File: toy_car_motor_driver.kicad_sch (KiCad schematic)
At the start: 10 parts, among them J1 Conn_01x06_Pin, J3 Conn_01x02_Pin, J4 Screw_Terminal_01x02, J5 Screw_Terminal_01x02, J6 Screw_Terminal_01x02, U1 L293D

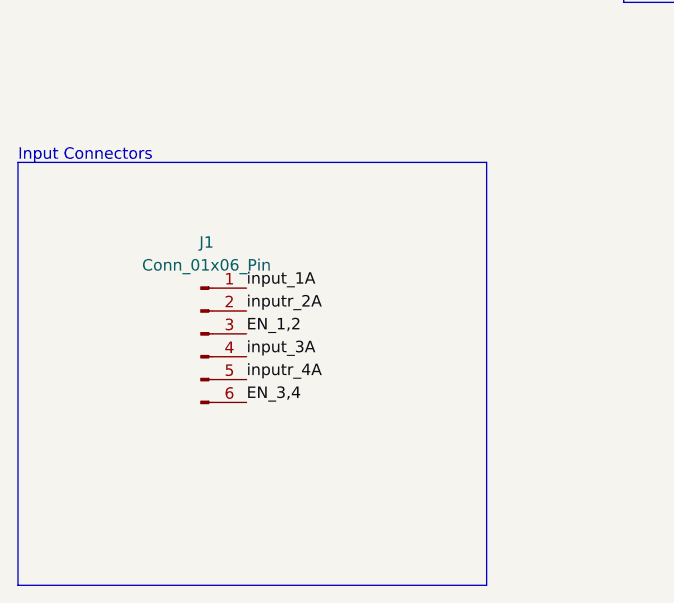
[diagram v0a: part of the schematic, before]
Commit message: added switches
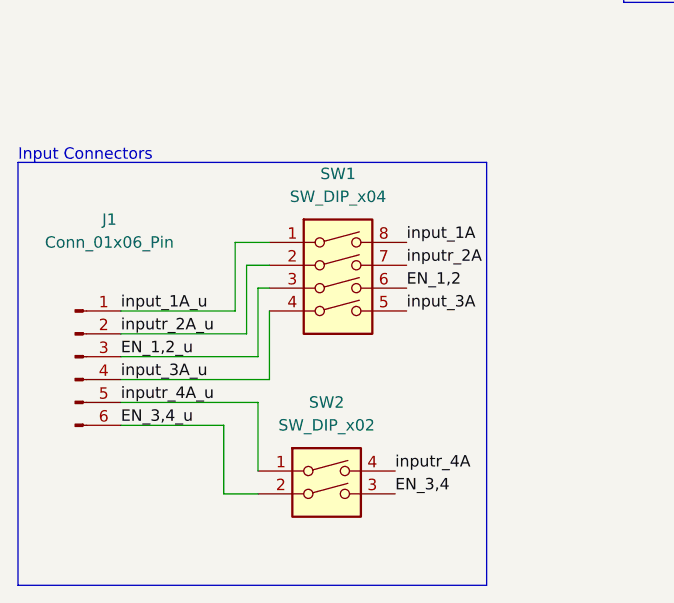
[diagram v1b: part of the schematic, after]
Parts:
- added SW1: SW_DIP_x04, symbol Switch:SW_DIP_x04
- added SW2: SW_DIP_x02, symbol Switch:SW_DIP_x02
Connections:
- net EN_1,2: now also SW1.6; no longer J1.3 (Pin_3)
- net EN_3,4: now also SW2.3; no longer J1.6 (Pin_6)
- net input_1A: now also SW1.8; no longer J1.1 (Pin_1)
- net input_3A: now also SW1.5; no longer J1.4 (Pin_4)
- net inputr_2A: now also SW1.7; no longer J1.2 (Pin_2)
- net inputr_4A: now also SW2.4; no longer J1.5 (Pin_5)
- new net EN_1,2_u: J1.3 (Pin_3), SW1.3
- new net EN_3,4_u: J1.6 (Pin_6), SW2.2
- new net input_1A_u: J1.1 (Pin_1), SW1.1
- new net input_3A_u: J1.4 (Pin_4), SW1.4
- new net inputr_2A_u: J1.2 (Pin_2), SW1.2
- new net inputr_4A_u: J1.5 (Pin_5), SW2.1
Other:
- moved on the sheet: J1
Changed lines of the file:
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@@
+    (stroke (width 0) (type default))
+  )
+  (wire (pts (xy 67.31 148.59) (xy 67.31 156.21))
     (stroke (width 0) (type default))
   )
@@
     (stroke (width 0) (type default))
   )
+  (wire (pts (xy 67.31 161.29) (xy 52.07 161.29))
+    (stroke (width 0) (type default))
+  )
   (wire (pts (xy 142.24 92.71) (xy 142.24 97.79))
     (stroke (width 0) (type default))
   )
+  (wire (pts (xy 63.5 163.83) (xy 52.07 163.83))
+    (stroke (width 0) (type default))
+  )
   (wire (pts (xy 224.79 78.74) (xy 224.79 80.01))
     (stroke (width 0) (type default))
@@
     (stroke (width 0) (type default))
   )
+  (wire (pts (xy 67.31 156.21) (xy 52.07 156.21))
+    (stroke (width 0) (type default))
+  )
   (wire (pts (xy 144.78 92.71) (xy 144.78 99.06))
     (stroke (width 0) (type default))
@@
     (stroke (width 0) (type default))
   )
+  (wire (pts (xy 67.31 168.91) (xy 67.31 161.29))
+    (stroke (width 0) (type default))
+  )
+  (wire (pts (xy 66.04 153.67) (xy 52.07 153.67))
+    (stroke (width 0) (type default))
+  )
   (wire (pts (xy 224.79 66.04) (xy 233.68 66.04))
     (stroke (width 0) (type default))
   )
+  (wire (pts (xy 67.31 171.45) (xy 63.5 171.45))
+    (stroke (width 0) (type default))
+  )
   (wire (pts (xy 139.7 104.14) (xy 139.7 101.6))
     (stroke (width 0) (type default))
   )
+  (wire (pts (xy 68.58 146.05) (xy 66.04 146.05))
+    (stroke (width 0) (type default))
+  )
   (wire (pts (xy 224.79 50.8) (xy 227.33 50.8))
     (stroke (width 0) (type default))
@@
     (stroke (width 0) (type default))
   )
+  (wire (pts (xy 68.58 148.59) (xy 67.31 148.59))
+    (stroke (width 0) (type default))
+  )
   (wire (pts (xy 142.24 39.37) (xy 142.24 41.91))
     (stroke (width 0) (type default))
@@
     (stroke (width 0) (type default))
   )
+  (wire (pts (xy 68.58 143.51) (xy 64.77 143.51))
+    (stroke (width 0) (type default))
+  )
   (wire (pts (xy 217.17 39.37) (xy 224.79 39.37))
     (stroke (width 0) (type default))
@@
     (stroke (width 0) (type default))
   )
+  (wire (pts (xy 68.58 151.13) (xy 68.58 158.75))
+    (stroke (width 0) (type default))
+  )
+  (wire (pts (xy 63.5 171.45) (xy 63.5 163.83))
+    (stroke (width 0) (type default))
+  )
+  (wire (pts (xy 68.58 158.75) (xy 52.07 158.75))
+    (stroke (width 0) (type default))
+  )
+  (wire (pts (xy 66.04 146.05) (xy 66.04 153.67))
+    (stroke (width 0) (type default))
+  )
+  (wire (pts (xy 64.77 143.51) (xy 64.77 151.13))
+    (stroke (width 0) (type default))
+  )
   (wire (pts (xy 139.7 92.71) (xy 139.7 97.79))
     (stroke (width 0) (type default))
@@
     (stroke (width 0) (type default))
   )
+  (wire (pts (xy 64.77 151.13) (xy 52.07 151.13))
+    (stroke (width 0) (type default))
+  )
   (wire (pts (xy 144.78 99.06) (xy 139.7 99.06))
     (stroke (width 0) (type default))
@@
     (effects (font (size 1.27 1.27)) (justify right bottom))
   )
-  (label "input_3A" (at 66.04 156.21 0) (fields_autoplaced)
+  (label "input_3A" (at 83.82 151.13 0) (fields_autoplaced)
+    (effects (font (size 1.27 1.27)) (justify left bottom))
+  )
+  (label "input_1A_u" (at 52.07 151.13 0) (fields_autoplaced)
     (effects (font (size 1.27 1.27)) (justify left bottom))
   )
@@
     (effects (font (size 1.27 1.27)) (justify right bottom))
   )
+  (label "EN_3,4_u" (at 52.07 163.83 0) (fields_autoplaced)
+    (effects (font (size 1.27 1.27)) (justify left bottom))
+  )
   (label "output_1" (at 152.4 57.15 0) (fields_autoplaced)
     (effects (font (size 1.27 1.27)) (justify left bottom))
   )
+  (label "inputr_4A_u" (at 52.07 161.29 0) (fields_autoplaced)
+    (effects (font (size 1.27 1.27)) (justify left bottom))
+  )
   (label "5V" (at 60.96 59.69 0) (fields_autoplaced)
     (effects (font (size 1.27 1.27)) (justify left bottom))
@@
     (effects (font (size 1.27 1.27)) (justify left bottom))
   )
-  (label "inputr_2A" (at 66.04 151.13 0) (fields_autoplaced)
+  (label "input_3A_u" (at 52.07 158.75 0) (fields_autoplaced)
+    (effects (font (size 1.27 1.27)) (justify left bottom))
+  )
+  (label "inputr_2A" (at 83.82 146.05 0) (fields_autoplaced)
     (effects (font (size 1.27 1.27)) (justify left bottom))
   )
@@
     (effects (font (size 1.27 1.27)) (justify right bottom))
   )
-  (label "EN_3,4" (at 66.04 161.29 0) (fields_autoplaced)
-    (effects (font (size 1.27 1.27)) (justify left bottom))
-  )
-  (label "input_1A" (at 66.04 148.59 0) (fields_autoplaced)
-    (effects (font (size 1.27 1.27)) (justify left bottom))
-  )
-  (label "inputr_4A" (at 66.04 158.75 0) (fields_autoplaced)
+  (label "EN_3,4" (at 82.55 171.45 0) (fields_autoplaced)
+    (effects (font (size 1.27 1.27)) (justify left bottom))
+  )
+  (label "input_1A" (at 83.82 143.51 0) (fields_autoplaced)
+    (effects (font (size 1.27 1.27)) (justify left bottom))
+  )
+  (label "inputr_4A" (at 82.55 168.91 0) (fields_autoplaced)
     (effects (font (size 1.27 1.27)) (justify left bottom))
   )
@@
     (effects (font (size 1.27 1.27)) (justify left bottom))
   )
+  (label "inputr_2A_u" (at 52.07 153.67 0) (fields_autoplaced)
+    (effects (font (size 1.27 1.27)) (justify left bottom))
+  )
   (label "outputr_1" (at 224.79 53.34 180) (fields_autoplaced)
     (effects (font (size 1.27 1.27)) (justify right bottom))
@@
     (effects (font (size 1.27 1.27)) (justify left bottom))
   )
-  (label "EN_1,2" (at 66.04 153.67 0) (fields_autoplaced)
+  (label "EN_1,2_u" (at 52.07 156.21 0) (fields_autoplaced)
+    (effects (font (size 1.27 1.27)) (justify left bottom))
+  )
+  (label "EN_1,2" (at 83.82 148.59 0) (fields_autoplaced)
     (effects (font (size 1.27 1.27)) (justify left bottom))
   )
@@
     )
   )
-  (symbol (lib_id "Connector:Conn_01x06_Pin") (at 60.96 153.67 0) (unit 1)
-    (in_bom yes) (on_board yes) (dnp no) (fields_autoplaced)
-    (property "Reference" "J1" (at 61.595 143.51 0)
-      (effects (font (size 1.27 1.27)))
-    )
-    (property "Value" "Conn_01x06_Pin" (at 61.595 146.05 0)
-      (effects (font (size 1.27 1.27)))
-    )
-    (property "Footprint" "" (at 60.96 153.67 0)
-      (effects (font (size 1.27 1.27)) hide)
-    )
-    (property "Datasheet" "~" (at 60.96 153.67 0)
+  (symbol (lib_id "Connector:Conn_01x06_Pin") (at 46.99 156.21 0) (unit 1)
+    (in_bom yes) (on_board yes) (dnp no)
+    (property "Reference" "J1" (at 50.8 140.97 0)
+      (effects (font (size 1.27 1.27)))
+    )
+    (property "Value" "Conn_01x06_Pin" (at 50.8 143.51 0)
+      (effects (font (size 1.27 1.27)))
+    )
+    (property "Footprint" "" (at 46.99 156.21 0)
+      (effects (font (size 1.27 1.27)) hide)
+    )
+    (property "Datasheet" "~" (at 46.99 156.21 0)
       (effects (font (size 1.27 1.27)) hide)
     )
@@
         (path "/bc5f8e62-44a0-4042-9de8-d5bf7b9ab401"
           (reference "#PWR05") (unit 1)
+        )
+      )
+    )
+  )
+  (symbol (lib_id "Switch:SW_DIP_x04") (at 76.2 148.59 0) (unit 1)
+    (in_bom yes) (on_board yes) (dnp no) (fields_autoplaced)
+    (property "Reference" "SW1" (at 76.2 135.89 0)
+      (effects (font (size 1.27 1.27)))
+    )
+    (property "Value" "SW_DIP_x04" (at 76.2 138.43 0)
+      (effects (font (size 1.27 1.27)))
+    )
+    (property "Footprint" "" (at 76.2 148.59 0)
+      (effects (font (size 1.27 1.27)) hide)
+    )
+    (property "Datasheet" "~" (at 76.2 148.59 0)
+      (effects (font (size 1.27 1.27)) hide)
+    )
+    (pin "3")
+    (pin "1")
+    (pin "5")
+    (pin "6")
+    (pin "4")
+    (pin "7")
+    (pin "8")
+    (pin "2")
+    (instances
+      (project "toy_car_motor_driver"
+        (path "/bc5f8e62-44a0-4042-9de8-d5bf7b9ab401"
+          (reference "SW1") (unit 1)
         )
       )
@@
         )
       )
+    )
+  )
+  (symbol (lib_id "Switch:SW_DIP_x02") (at 74.93 171.45 0) (unit 1)
+    (in_bom yes) (on_board yes) (dnp no) (fields_autoplaced)
+    (property "Reference" "SW2" (at 74.93 161.29 0)
+      (effects (font (size 1.27 1.27)))
+    )
+    (property "Value" "SW_DIP_x02" (at 74.93 163.83 0)
+      (effects (font (size 1.27 1.27)))
+    )
+    (property "Footprint" "" (at 74.93 171.45 0)
+      (effects (font (size 1.27 1.27)) hide)
+    )
+    (property "Datasheet" "~" (at 74.93 171.45 0)
+      (effects (font (size 1.27 1.27)) hide)
+    )
+    (pin "3")
+    (pin "4")
+    (pin "2")
+    (pin "1")
+    (instances
+      (project "toy_car_motor_driver"
+        (path "/bc5f8e62-44a0-4042-9de8-d5bf7b9ab401"
+          (reference "SW2") (unit 1)
+        )
+      )

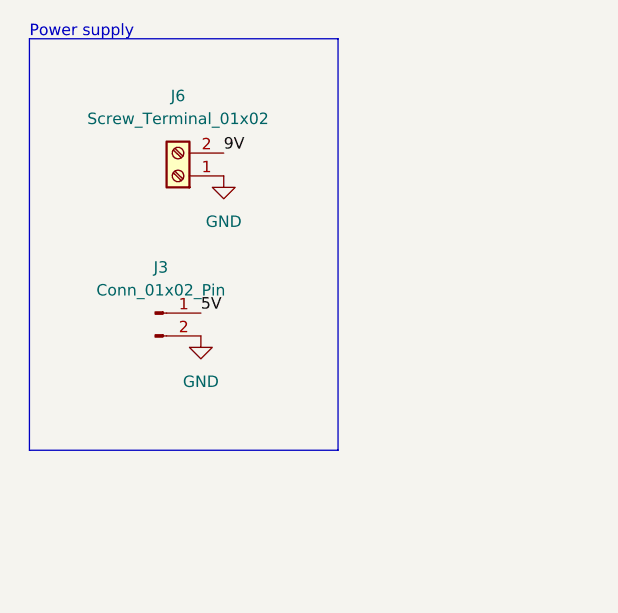
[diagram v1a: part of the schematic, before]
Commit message: Added switches for input power
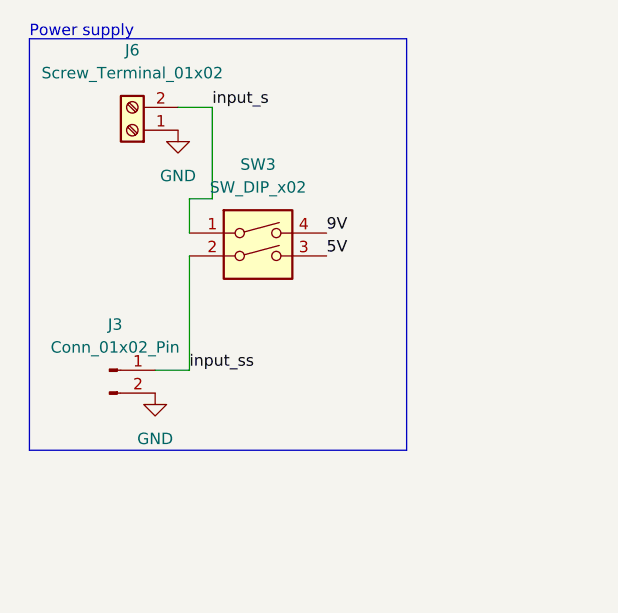
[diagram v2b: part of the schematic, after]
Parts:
- added SW3: SW_DIP_x02, symbol Switch:SW_DIP_x02
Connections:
- net 5V: now also SW3.3; no longer J3.1 (Pin_1)
- net 9V: now also SW3.4; no longer J6.2 (Pin_2)
- new net input_s: J6.2 (Pin_2), SW3.1
- new net input_ss: J3.1 (Pin_1), SW3.2
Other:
- moved on the sheet: J3, J6
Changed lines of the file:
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@@
+    (stroke (width 0) (type default))
+  )
+  (wire (pts (xy 59.69 50.8) (xy 59.69 46.99))
+    (stroke (width 0) (type default))
+  )
+  (wire (pts (xy 62.23 46.99) (xy 62.23 36.83))
+    (stroke (width 0) (type default))
+  )
+  (wire (pts (xy 58.42 36.83) (xy 62.23 36.83))
     (stroke (width 0) (type default))
   )
@@
     (stroke (width 0) (type default))
   )
+  (wire (pts (xy 59.69 46.99) (xy 62.23 46.99))
+    (stroke (width 0) (type default))
+  )
   (wire (pts (xy 68.58 146.05) (xy 66.04 146.05))
     (stroke (width 0) (type default))
@@
     (stroke (width 0) (type default))
   )
+  (wire (pts (xy 59.69 53.34) (xy 59.69 66.04))
+    (stroke (width 0) (type default))
+  )
   (wire (pts (xy 137.16 41.91) (xy 137.16 46.99))
     (stroke (width 0) (type default))
@@
     (stroke (width 0) (type default))
   )
+  (wire (pts (xy 59.69 66.04) (xy 55.88 66.04))
+    (stroke (width 0) (type default))
+  )
   (wire (pts (xy 139.7 92.71) (xy 139.7 97.79))
     (stroke (width 0) (type default))
@@
     (fill (type none))
   )
-  (rectangle (start 41.91 29.21) (end 76.2 74.93)
+  (rectangle (start 41.91 29.21) (end 83.82 74.93)
     (stroke (width 0) (type default))
     (fill (type none))
@@
     (effects (font (size 1.27 1.27)) (justify left bottom))
   )
-  (label "5V" (at 60.96 59.69 0) (fields_autoplaced)
+  (label "5V" (at 74.93 53.34 0) (fields_autoplaced)
     (effects (font (size 1.27 1.27)) (justify left bottom))
   )
@@
     (effects (font (size 1.27 1.27)) (justify left bottom))
   )
-  (label "9V" (at 63.5 41.91 0) (fields_autoplaced)
+  (label "9V" (at 74.93 50.8 0) (fields_autoplaced)
     (effects (font (size 1.27 1.27)) (justify left bottom))
   )
@@
     (effects (font (size 1.27 1.27)) (justify right bottom))
   )
+  (label "input_ss" (at 59.69 66.04 0) (fields_autoplaced)
+    (effects (font (size 1.27 1.27)) (justify left bottom))
+  )
   (label "outputr_1" (at 152.4 62.23 0) (fields_autoplaced)
     (effects (font (size 1.27 1.27)) (justify left bottom))
@@
   (label "EN_1,2" (at 127 67.31 180) (fields_autoplaced)
     (effects (font (size 1.27 1.27)) (justify right bottom))
+  )
+  (label "input_s" (at 62.23 36.83 0) (fields_autoplaced)
+    (effects (font (size 1.27 1.27)) (justify left bottom))
   )
   (label "output_2" (at 152.4 72.39 0) (fields_autoplaced)
@@
     )
   )
+  (symbol (lib_id "Switch:SW_DIP_x02") (at 67.31 53.34 0) (unit 1)
+    (in_bom yes) (on_board yes) (dnp no) (fields_autoplaced)
+    (property "Reference" "SW3" (at 67.31 43.18 0)
+      (effects (font (size 1.27 1.27)))
+    )
+    (property "Value" "SW_DIP_x02" (at 67.31 45.72 0)
+      (effects (font (size 1.27 1.27)))
+    )
+    (property "Footprint" "" (at 67.31 53.34 0)
+      (effects (font (size 1.27 1.27)) hide)
+    )
+    (property "Datasheet" "~" (at 67.31 53.34 0)
+      (effects (font (size 1.27 1.27)) hide)
+    )
+    (pin "3")
+    (pin "4")
+    (pin "2")
+    (pin "1")
+    (instances
+      (project "toy_car_motor_driver"
+        (path "/bc5f8e62-44a0-4042-9de8-d5bf7b9ab401"
+          (reference "SW3") (unit 1)
+        )
+      )
+    )
+  )
   (symbol (lib_id "Connector:Screw_Terminal_01x02") (at 232.41 50.8 0) (unit 1)
     (in_bom yes) (on_board yes) (dnp no) (fields_autoplaced)
@@
     )
   )
-  (symbol (lib_id "power:GND") (at 63.5 44.45 0) (unit 1)
-    (in_bom yes) (on_board yes) (dnp no) (fields_autoplaced)
-    (property "Reference" "#PWR03" (at 63.5 50.8 0)
-      (effects (font (size 1.27 1.27)) hide)
-    )
-    (property "Value" "GND" (at 63.5 49.53 0)
-      (effects (font (size 1.27 1.27)))
-    )
-    (property "Footprint" "" (at 63.5 44.45 0)
-      (effects (font (size 1.27 1.27)) hide)
-    )
-    (property "Datasheet" "" (at 63.5 44.45 0)
+  (symbol (lib_id "power:GND") (at 58.42 39.37 0) (unit 1)
+    (in_bom yes) (on_board yes) (dnp no) (fields_autoplaced)
+    (property "Reference" "#PWR03" (at 58.42 45.72 0)
+      (effects (font (size 1.27 1.27)) hide)
+    )
+    (property "Value" "GND" (at 58.42 44.45 0)
+      (effects (font (size 1.27 1.27)))
+    )
+    (property "Footprint" "" (at 58.42 39.37 0)
+      (effects (font (size 1.27 1.27)) hide)
+    )
+    (property "Datasheet" "" (at 58.42 39.37 0)
       (effects (font (size 1.27 1.27)) hide)
     )
@@
     )
   )
-  (symbol (lib_id "Connector:Conn_01x02_Pin") (at 55.88 59.69 0) (unit 1)
-    (in_bom yes) (on_board yes) (dnp no) (fields_autoplaced)
-    (property "Reference" "J3" (at 56.515 54.61 0)
-      (effects (font (size 1.27 1.27)))
-    )
-    (property "Value" "Conn_01x02_Pin" (at 56.515 57.15 0)
-      (effects (font (size 1.27 1.27)))
-    )
-    (property "Footprint" "" (at 55.88 59.69 0)
-      (effects (font (size 1.27 1.27)) hide)
-    )
-    (property "Datasheet" "~" (at 55.88 59.69 0)
+  (symbol (lib_id "Connector:Conn_01x02_Pin") (at 50.8 66.04 0) (unit 1)
+    (in_bom yes) (on_board yes) (dnp no) (fields_autoplaced)
+    (property "Reference" "J3" (at 51.435 60.96 0)
+      (effects (font (size 1.27 1.27)))
+    )
+    (property "Value" "Conn_01x02_Pin" (at 51.435 63.5 0)
+      (effects (font (size 1.27 1.27)))
+    )
+    (property "Footprint" "" (at 50.8 66.04 0)
+      (effects (font (size 1.27 1.27)) hide)
+    )
+    (property "Datasheet" "~" (at 50.8 66.04 0)
       (effects (font (size 1.27 1.27)) hide)
     )
@@
     )
   )
-  (symbol (lib_id "Connector:Screw_Terminal_01x02") (at 58.42 44.45 180) (unit 1)
-    (in_bom yes) (on_board yes) (dnp no) (fields_autoplaced)
-    (property "Reference" "J6" (at 58.42 35.56 0)
-      (effects (font (size 1.27 1.27)))
-    )
-    (property "Value" "Screw_Terminal_01x02" (at 58.42 38.1 0)
-      (effects (font (size 1.27 1.27)))
-    )
-    (property "Footprint" "" (at 58.42 44.45 0)
-      (effects (font (size 1.27 1.27)) hide)
-    )
-    (property "Datasheet" "~" (at 58.42 44.45 0)
+  (symbol (lib_id "Connector:Screw_Terminal_01x02") (at 53.34 39.37 180) (unit 1)
+    (in_bom yes) (on_board yes) (dnp no) (fields_autoplaced)
+    (property "Reference" "J6" (at 53.34 30.48 0)
+      (effects (font (size 1.27 1.27)))
+    )
+    (property "Value" "Screw_Terminal_01x02" (at 53.34 33.02 0)
+      (effects (font (size 1.27 1.27)))
+    )
+    (property "Footprint" "" (at 53.34 39.37 0)
+      (effects (font (size 1.27 1.27)) hide)
+    )
+    (property "Datasheet" "~" (at 53.34 39.37 0)
       (effects (font (size 1.27 1.27)) hide)
     )
@@
     )
   )
-  (symbol (lib_id "power:GND") (at 60.96 62.23 0) (unit 1)
-    (in_bom yes) (on_board yes) (dnp no) (fields_autoplaced)
-    (property "Reference" "#PWR02" (at 60.96 68.58 0)
-      (effects (font (size 1.27 1.27)) hide)
-    )
-    (property "Value" "GND" (at 60.96 67.31 0)
-      (effects (font (size 1.27 1.27)))
-    )
-    (property "Footprint" "" (at 60.96 62.23 0)
-      (effects (font (size 1.27 1.27)) hide)
-    )
-    (property "Datasheet" "" (at 60.96 62.23 0)
-      (effects (font (size 1.27 1.27)) hide)
-    )
+  (symbol (lib_id "power:GND") (at 55.88 68.58 0) (unit 1)
+    (in_bom yes) (on_board yes) (dnp no) (fields_autoplaced)
+    (property "Reference" "#PWR02" (at 55.88 74.93 0)
+      (effects (font (size 1.27 1.27)) hide)
+    )
+    (property "Value" "GND" (at 55.88 73.66 0)
+      (effects (font (size 1.27 1.27)))
+    )
+    (property "Footprint" "" (at 55.88 68.58 0)
+      (effects (font (size 1.27 1.27)) hide)
+    )
+    (property "Datasheet" "" (at 55.88 68.58 0)
+      (effects (font (size 1.27 1.27)) hide)
+    )

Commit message: Completed pcb design and routing
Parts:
- removed SW2, SW3: SW_DIP_x02, symbol Switch:SW_DIP_x02
- added C5, C6: 0.1uF, Capacitor_THT:C_Disc_D3.8mm_W2.6mm_P2.50mm, symbol Device:C
- added D1: LED, LED_THT:LED_D3.0mm, symbol Device:LED
- added R1: 510, Resistor_THT:R_Axial_DIN0204_L3.6mm_D1.6mm_P7.62mm_Horizontal, symbol Device:R
- C1, C2, C3, C4: footprint (none) -> Capacitor_THT:C_Disc_D3.8mm_W2.6mm_P2.50mm
- J1: footprint (none) -> Connector_PinHeader_2.54mm:PinHeader_1x06_P2.54mm_Vertical
- J3: footprint (none) -> Connector_PinHeader_2.54mm:PinHeader_1x02_P2.54mm_Vertical
- J4, J5, J6: footprint (none) -> Connector:JWT_A3963_1x02_P3.96mm_Vertical
- SW1: footprint (none) -> Package_DIP:DIP-8_W7.62mm
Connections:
- net EN_3,4_u is gone; now on net EN_3,4: J1.6 (Pin_6)
- net input_s is gone; now on net GND_i: J6.2 (Pin_2)
- net input_ss is gone; now on net 5V_i: J3.1 (Pin_1)
- net inputr_4A_u is gone; now on net inputr_4A: J1.5 (Pin_5)
- net 5V: now also SW1.6, C5.2
- net 9V: now also SW1.8, C6.1, R1.2
- net EN_1,2: now also J1.3 (Pin_3); no longer SW1.6
- net GND: now also SW1.5, SW1.7, C5.1, C6.2, D1.1 (K); no longer J3.2 (Pin_2), J6.1 (Pin_1)
- net input_1A: now also J1.1 (Pin_1); no longer SW1.8
- net input_3A: now also J1.4 (Pin_4); no longer SW1.5
- net inputr_2A: now also J1.2 (Pin_2); no longer SW1.7
- net EN_1,2_u renamed 5V_i
- net 5V_i: no longer J1.3 (Pin_3)
- net input_1A_u renamed GND_i
- net GND_i: now also J3.2 (Pin_2), SW1.4; no longer J1.1 (Pin_1)
- removed net input_3A_u: J1.4 (Pin_4), SW1.4
- net inputr_2A_u renamed 9V_i
- net 9V_i: now also J6.1 (Pin_1); no longer J1.2 (Pin_2)
- new net: D1.2 (A), R1.1
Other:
- moved on the sheet: J1, J6, SW1
